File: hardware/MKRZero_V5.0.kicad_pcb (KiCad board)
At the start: 2 copper layers, 80 x 60 mm, 55 parts, among them IC1 PCF8523T, IC2 CR1220-2, J1 USB_B_Micro, J2 2X3_SMD_MALE, J3 AMPHENOL_114-00841-68, J6 Conn_01x08_Pin, J7 Conn_01x04_Pin, J8 PJ-320A, Q1 32.768KHz, SW1 RotaryEncoder_Switch_MP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

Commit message: midi connector corrections, use MG03254F-RA magnetic pogo 3pin connector
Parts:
- J7: value Conn_01x04_Pin -> Conn_01x03_Pin; footprint Connector_JST:JST_SH_SM04B-SRSS-TB_1x04-1MP_P1.00mm_Horizontal -> MKRZero_V5.0:MG03254F-RA
- moved J7 2.50 mm to (74.5, 45.0), turned to -90 degrees
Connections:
- J7 pad 3: unconnected-(J7-Pin_3-Pad3) -> GND
- JMIDIIN1 pad 4: Net-(JMIDIIN1-Pad4) -> Net-(D4-A)
- JMIDIIN1 pad 5: Net-(D4-A) -> Net-(JMIDIIN1-Pad5)
- R10 pad 1: Net-(JMIDIIN1-Pad4) -> Net-(JMIDIIN1-Pad5)
- R11 pad 1: Net-(JMIDIOUT1-Pad4) -> Net-(JMIDIOUT1-Pad5)
- R12 pad 2: Net-(JMIDIOUT1-Pad5) -> Net-(JMIDIOUT1-Pad4)
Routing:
- net Net-(JMIDIIN1-Pad5): track 0.00 -> 11.2 mm
- net Net-(JMIDIIN1-Pad4): track 11.2 -> 0.00 mm
- net Net-(JMIDIOUT1-Pad5): track 11.7 -> 19.9 mm
- net Net-(D4-A): track 21.3 -> 26.3 mm
- net /PA22_TC4-W0: track 72.2 -> 67.7 mm
- net +5V: track 79.7 -> 77.7 mm
- net Net-(JMIDIOUT1-Pad4): track 13.8 -> 15.1 mm, vias 0 -> 1
- net GND: vias 257 -> 283
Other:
- board text added: "v 1.1"

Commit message: midi still not working
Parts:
- added C15: .1uF, Capacitor_SMD:C_0805_2012Metric, F.Cu at (41.1, 11.7)
- added U4: W25Q128JVS, Package_SO:SOIC-8W_5.3x5.3mm_P1.27mm, F.Cu at (47.2, 10.9)
- J2: moved to F.Cu
- moved J2 26.7 mm to (25.7, 14.9), turned to 180 degrees
- moved R4 26.1 mm to (30.0, 20.4)
- moved R3 25.2 mm to (26.9, 20.4)
- moved D4 16.9 mm to (16.6, 31.5), turned to -90 degrees
- moved R10 12.2 mm to (18.3, 29.5), turned to -90 degrees
- moved J3 1.73 mm to (5.53, 46.5)
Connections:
- SW1 pad B: /PA19_S1_MISO -> /PA04_AIN4
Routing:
- net /PA19_S1_MISO: track 38.8 -> 6.95 mm, vias 1 -> 0
- net /PA04_AIN4: track 0.00 -> 30.0 mm
- net /PA31_SWDIO: track 40.2 -> 11.7 mm, vias 1 -> 2
- net /RESETN: track 45.3 -> 17.6 mm, vias 0 -> 2
- net Net-(J2-Pad5): track 36.5 -> 10.2 mm, vias 1 -> 0
- net /PA30_SWCLK: track 41.0 -> 19.0 mm, vias 1 -> 0
- net /PA22_TC4-W0: track 67.7 -> 46.7 mm, vias 0 -> 1
- net /PB03_AIN11: track 0.00 -> 18.9 mm, vias 0 -> 2
- net /PA06_AIN6: track 36.2 -> 52.9 mm, vias 0 -> 1
- net /PA14_S2_NSS: track 114.3 -> 97.7 mm, vias 2 -> 3
- net /PB22_S5_TX: track 27.6 -> 17.2 mm, vias 2 -> 0
- net /PA05_AIN5: track 33.2 -> 40.4 mm
- net +3V3: track 194.6 -> 200.5 mm, vias 3 -> 7
- net Net-(D4-K): track 12.1 -> 6.23 mm
- net +5V: track 77.7 -> 72.4 mm
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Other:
- board size 80 x 60 mm -> 81.4 x 60 mm
- copper layers 2 -> 4
- board text added: "3v"
- board text added: "GND"
- board text added: "RESET"
- board text added: "SWDCLK"
- board text added: "SWDIO"
- board text added: "v 1.2"
- board text removed: "nicnewdigate@gmail.com"
- board text removed: "v 1.1"

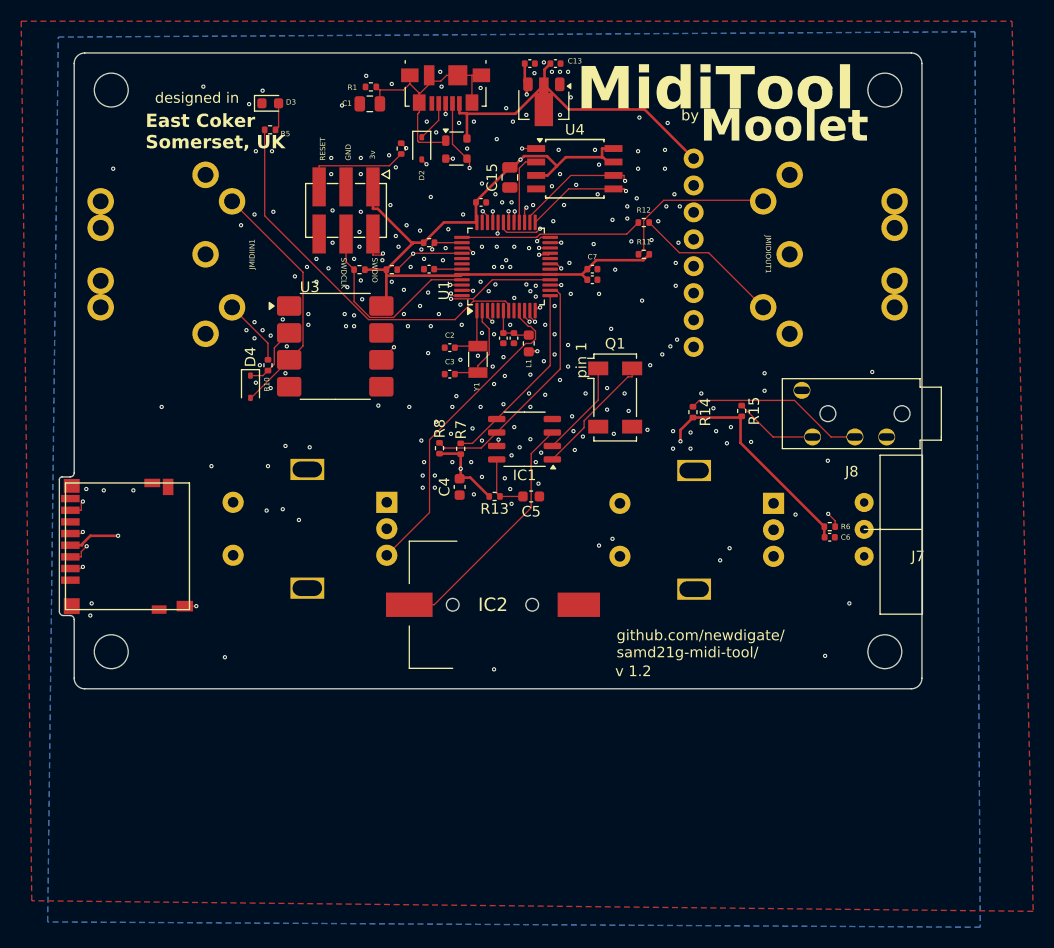
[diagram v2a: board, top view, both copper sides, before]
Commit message: v1.3 hopefully midi in will work this time?
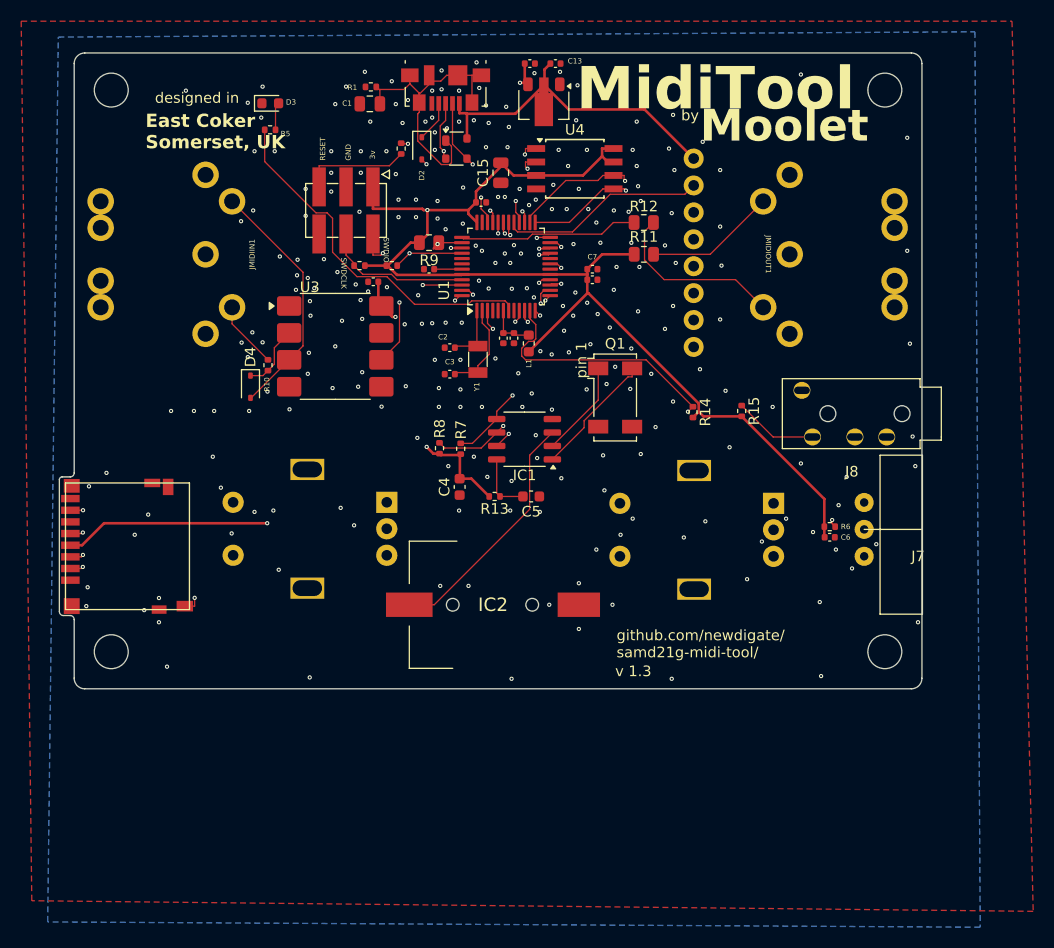
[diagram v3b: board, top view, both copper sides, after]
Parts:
- added C16: 100nF, Capacitor_SMD:C_0402_1005Metric, F.Cu at (28.2, 21.6)
- R11, R12: value 220 -> 47; footprint Resistor_SMD:R_0402_1005Metric -> Resistor_SMD:R_0805_2012Metric
- R9: value 1k -> 470; footprint Resistor_SMD:R_0402_1005Metric -> Resistor_SMD:R_0805_2012Metric
- moved C15 0.96 mm to (40.3, 11.3)
- moved R3 0.38 mm to (26.9, 20.1)
- moved R4 0.38 mm to (30.0, 20.1)
- turned R12 to 180 degrees
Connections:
- JMIDIIN1 pad 4: Net-(D4-A) -> Net-(JMIDIIN1-Pad4)
- JMIDIIN1 pad 5: Net-(JMIDIIN1-Pad5) -> Net-(D4-A)
- JMIDIOUT1 pad 2: unconnected-(JMIDIOUT1-Pad2) -> GND
- R10 pad 1: Net-(JMIDIIN1-Pad5) -> Net-(JMIDIIN1-Pad4)
- R11 pad 1: Net-(JMIDIOUT1-Pad5) -> +3V3
- R11 pad 2: +3V3 -> Net-(JMIDIOUT1-Pad4)
- R12 pad 1: /PB22_S5_TX -> Net-(JMIDIOUT1-Pad5)
- R12 pad 2: Net-(JMIDIOUT1-Pad4) -> /PB22_S5_TX
- U3 pad 8: +3V3 -> +5V
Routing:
- net +5V: track 72.4 -> 105.0 mm, vias 0 -> 1
- net /PA06_AIN6: track 52.9 -> 40.9 mm
- net Net-(JMIDIIN1-Pad5): track 6.36 -> 0.00 mm
- net Net-(JMIDIIN1-Pad4): track 0.00 -> 6.36 mm
- net /PA30_SWCLK: track 19.0 -> 14.0 mm
- net /PA27_CD: track 46.7 -> 50.6 mm
- net Net-(D1-GND): track 24.2 -> 27.9 mm
- net /PB08_LED: track 36.6 -> 34.3 mm
- net /PA11_TCC0-W3: track 43.0 -> 45.2 mm
- net +3V3: track 200.5 -> 198.5 mm, vias 7 -> 4
- net /PA21_TCC0-W7: track 33.3 -> 31.5 mm
- net Net-(JMIDIOUT1-Pad4): track 14.1 -> 12.4 mm
- net Net-(JMIDIOUT1-Pad5): track 15.5 -> 16.9 mm
- net /PA07_AIN7: track 15.5 -> 14.7 mm
- net /PA09_S0_I2C_SCL: track 22.8 -> 22.1 mm, vias 0 -> 2
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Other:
- board text added: "v 1.3"
- board text removed: "v 1.2"
